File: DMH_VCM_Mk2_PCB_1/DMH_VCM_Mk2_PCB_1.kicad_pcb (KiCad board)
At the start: 2 copper layers, 48 x 175 mm, 95 parts, among them J1 TS_Jack_6.35mm_Sw, J10 TS_Jack_6.35mm_Sw, J100 IDC_02x05, J2 TS_Jack_6.35mm_Sw, J200 IDC_02x05, J3 TS_Jack_6.35mm_Sw, J4 TS_Jack_6.35mm_Sw, J5 TS_Jack_6.35mm_Sw, J50 Conn_01x08, J6 TS_Jack_6.35mm_Sw, J60 Conn_01x08, J7 TS_Jack_6.35mm_Sw, J70 Conn_01x08, J8 TS_Jack_6.35mm_Sw, J9 TS_Jack_6.35mm_Sw, Q1 BC548, Q2 BC548, Q3 BC548, Q4 BC548, Q5 BC548, Q6 BC548, U1 TL074, U2 TL074, U3 TL074

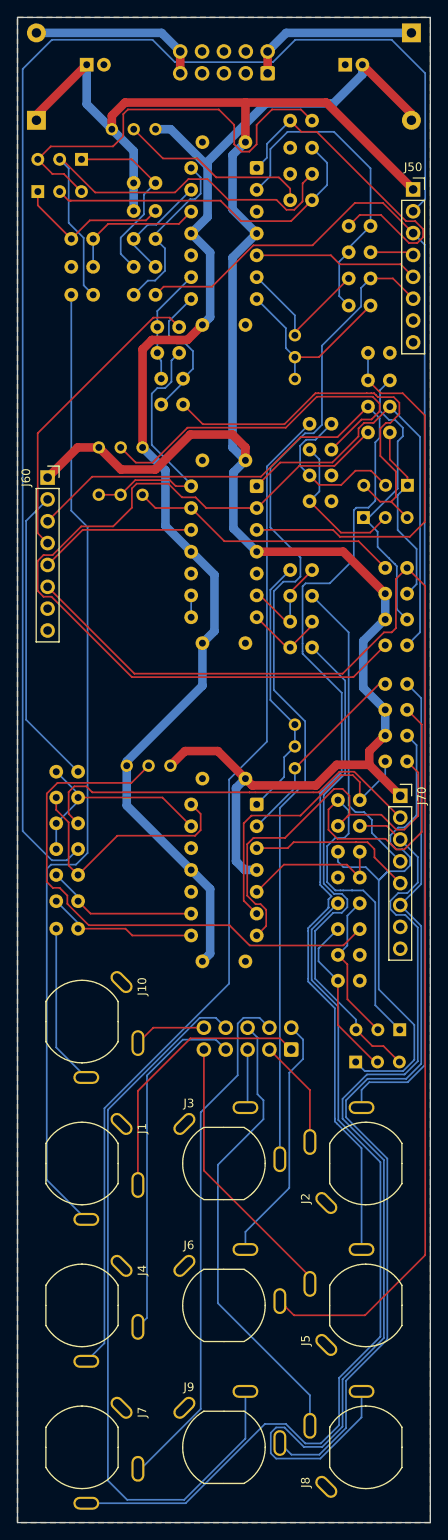
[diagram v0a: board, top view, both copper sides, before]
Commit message: Resolved J70 volume conflict
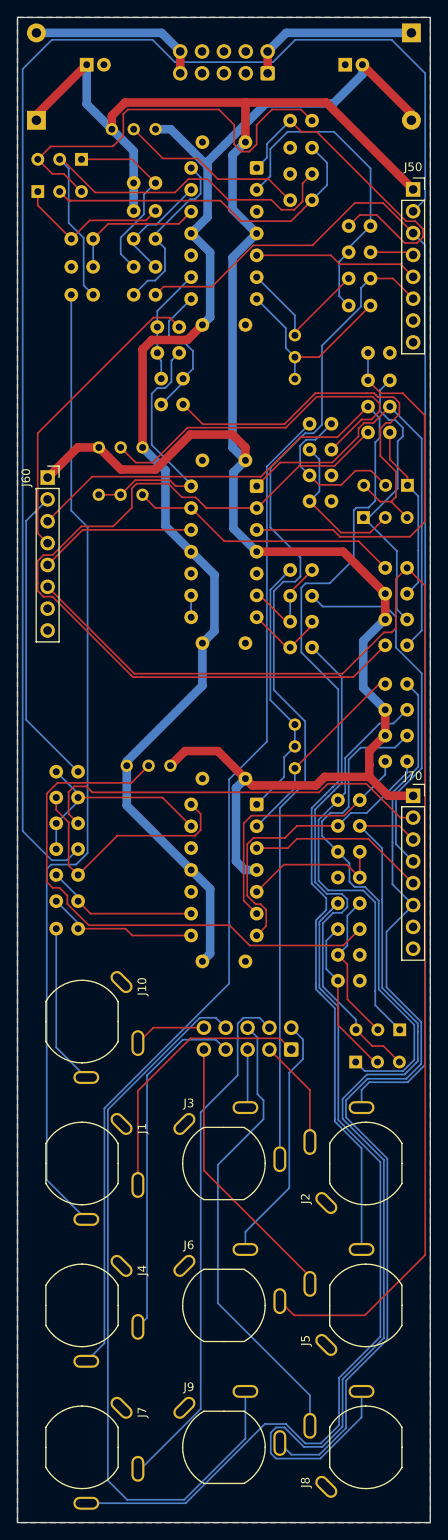
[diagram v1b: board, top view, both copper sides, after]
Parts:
- moved J70 1.50 mm to (97.0, 133.0)
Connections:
- J70 pad 7: GND -> unconnected-(J70-Pin_7-Pad7)
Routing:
- net Net-(Q5-C): track 65.7 -> 48.8 mm
- net Net-(R33-Pad1): track 47.8 -> 35.7 mm
- net /Inputs and Outputs/Offset C Pot: track 35.7 -> 42.5 mm
- net Net-(Q6-C): track 61.6 -> 58.0 mm
- net Net-(U3B--): track 35.1 -> 31.5 mm
- net /Inputs and Outputs/CV C Jack: track 109.0 -> 112.0 mm
- net +12V: track 240.6 -> 242.4 mm
- net /Inputs and Outputs/CV Amt C Pot: track 19.5 -> 20.8 mm
- net /Inputs and Outputs/Output C Jack: track 117.2 -> 118.4 mm
- net Net-(R9-Pad1): track 22.4 -> 21.6 mm
- net Net-(Q3-C): track 21.4 -> 20.7 mm
- net Net-(Q6-B): track 19.4 -> 18.7 mm
- net /Inputs and Outputs/Input C Jack: track 102.3 -> 101.5 mm
- net /Inputs and Outputs/Output B Jack: track 154.7 -> 154.0 mm

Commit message: Generated Gerbers
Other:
- board text added: "Mk2.0 - October 2025"
- board text removed: "Mk2.0 - Month 2025"
